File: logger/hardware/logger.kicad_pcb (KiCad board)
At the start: 4 copper layers, 56.6 x 27.9 mm, 44 parts, among them J2 USB_C_Receptacle_USB2.0_14P, J3 S5B-PH-SM4-TB(LF)(SN), J4 Conn_01x04, J5 Micro_SD_Card_Det2, Q1 2N7002K, SW1 SW_Push, SW2 SW_Push, U1 ESP32-S3-WROOM-1-N8, U2 TCAN330, U3 USBLC6-2P6, U4 TPS62172DSG

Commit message: Kicad updates and ignore
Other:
- board text added: "120 TERM"
- board text added: "BOOT"
- board text added: "RST"
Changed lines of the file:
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@@
 			(plot_on_all_layers_selection 0x00000000_00000000_00000000_00000000)
 			(disableapertmacros no)
-			(usegerberextensions no)
+			(usegerberextensions yes)
 			(usegerberattributes yes)
 			(usegerberadvancedattributes yes)
@@
 			(outputformat 1)
 			(mirror no)
-			(drillshape 1)
+			(drillshape 0)
 			(scaleselection 1)
 			(outputdirectory "")
@@
 			(at 3.646 -0.856 0)
 			(layer "F.SilkS")
+			(hide yes)
 			(effects
 				(font
@@
 			(at -0.89 2.344 0)
 			(layer "F.SilkS")
+			(hide yes)
 			(effects
 				(font
@@
 			)
 		)
-		(attr smd dnp)
+		(attr smd)
 		(duplicate_pad_numbers_are_jumpers no)
 		(fp_line
@@
 			(at 0 1.17 90)
 			(layer "B.SilkS")
+			(hide yes)
 			(effects
 				(font
@@
 		(layer "Edge.Cuts")
 	)
+	(gr_text "RST"
+		(at 146.7 82.6 0)
+		(layer "F.SilkS")
+		(effects
+			(font
+				(size 1 1)
+				(thickness 0.15)
+			)
+			(justify left bottom)
+		)
+	)
+	(gr_text "BOOT"
+		(at 131 81.9 90)
+		(layer "F.SilkS")
+		(effects
+			(font
+				(size 1 1)
+				(thickness 0.15)
+			)
+			(justify left bottom)
+		)
+	)
+	(gr_text "120\nTERM"
+		(at 121.315 81.5 0)
+		(layer "B.SilkS")
+		(effects
+			(font
+				(size 1 1)
+				(thickness 0.15)
+			)
+			(justify left bottom mirror)
+		)
+	)
 	(gr_text "3V3 OUT"

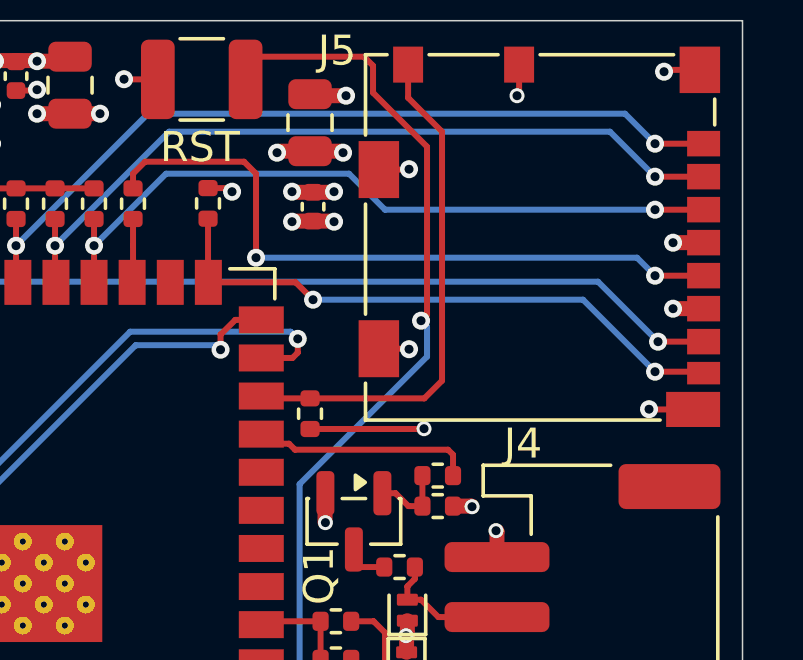
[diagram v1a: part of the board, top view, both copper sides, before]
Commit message: fix: I/O allocations on logger ESP32-S3
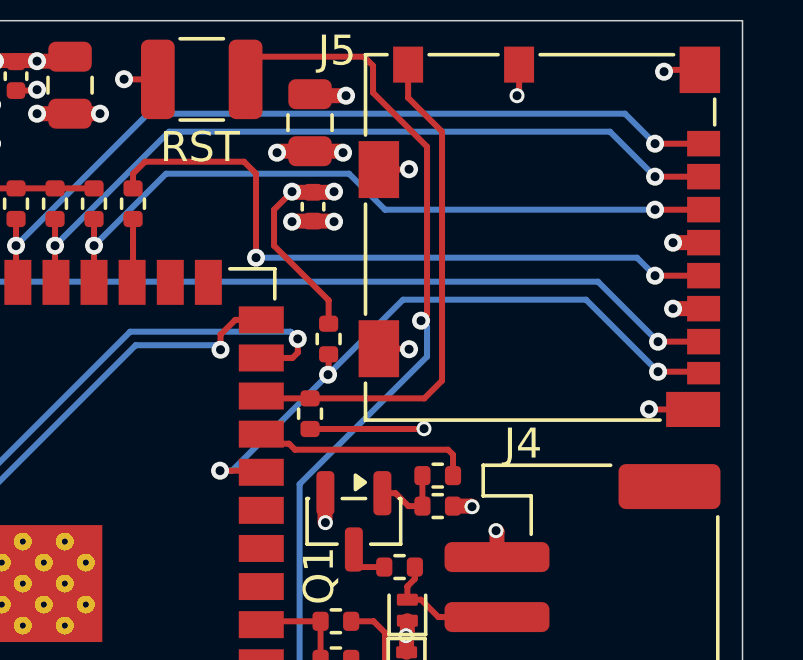
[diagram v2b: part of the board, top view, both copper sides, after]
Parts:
- U1: value ESP32-S3-WROOM-1-N8 -> ESP32-S3-WROOM-1-N4
- moved R11 6.05 mm to (152.3, 88.4)
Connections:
- U1 pad 10: unconnected-(U1-IO17-Pad10) -> Net-(J5-DAT1)
- U1 pad 15: Net-(J5-DAT1) -> unconnected-(U1-IO3-Pad15)
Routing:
- net +3.3V: track 31.0 -> 35.5 mm, vias 44 -> 43
- net Net-(J5-DAT1): track 19.9 -> 21.6 mm, vias 2 -> 3
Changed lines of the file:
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@@
 			(crossoutdnponfab yes)
 			(subtractmaskfromsilk no)
-			(outputformat 1)
+			(outputformat 4)
 			(mirror no)
 			(drillshape 0)
 			(scaleselection 1)
-			(outputdirectory "")
+			(outputdirectory "pdf")
 		)
 	)
@@
 	(footprint "Resistor_SMD:R_0402_1005Metric"
 		(layer "F.Cu")
-		(at 148.3 83.89 90)
+		(at 152.32 88.41 90)
 		(descr "Resistor SMD 0402 (1005 Metric), square (rectangular) end terminal, IPC-7351 nominal, (Body size source: IPC-SM-782 page 72, https://www.pcb-3d.com/wordpress/wp-content/uploads/ipc-sm-782a_amendment_1_and_2.pdf)")
 		(tags "resistor")
@@
 			)
 		)
-		(property "LCSC" "C7519"
+		(property "LCSC" "C15999"
 			(at 0 0 0)
 			(unlocked yes)
@@
 			)
 		)
-		(property "Value" "ESP32-S3-WROOM-1-N8"
+		(property "Value" "ESP32-S3-WROOM-1-N4"
 			(at 0 14.6 180)
 			(unlocked yes)
@@
 			)
 		)
-		(property "LCSC" "C2913198"
+		(property "LCSC" "C2913197"
 			(at 0 0 180)
 			(unlocked yes)
@@
 			(size 1.5 0.9)
 			(layers "F.Cu" "F.Mask" "F.Paste")
-			(net "unconnected-(U1-IO17-Pad10)")
+			(net "Net-(J5-DAT1)")
 			(pinfunction "IO17_10")
 			(pintype "bidirectional")
@@
 			(size 1.5 0.9)
 			(layers "F.Cu" "F.Mask" "F.Paste")
-			(net "Net-(J5-DAT1)")
+			(net "unconnected-(U1-IO3-Pad15)")
 			(pinfunction "IO3_15")
 			(pintype "bidirectional")
@@
 	)
 	(segment
-		(start 155.49 91.41)
-		(end 155.5 91.4)
+		(start 150.5 85.3)
+		(end 150.5 84.1)
 		(width 0.2)
 		(layer "F.Cu")
@@
 	)
 	(segment
-		(start 148.98 83.38)
-		(end 149.1 83.5)
+		(start 155.49 91.41)
+		(end 155.5 91.4)
 		(width 0.2)
 		(layer "F.Cu")
@@
 	)
 	(segment
+		(start 152.32 87.9)
+		(end 152.32 87.12)
+		(width 0.2)
+		(layer "F.Cu")
+		(net "+3.3V")
+	)
+	(segment
 		(start 151.7 91.41)
 		(end 155.49 91.41)
@@
 	)
 	(segment
-		(start 148.3 83.38)
-		(end 148.98 83.38)
+		(start 152.32 87.12)
+		(end 150.5 85.3)
+		(width 0.2)
+		(layer "F.Cu")
+		(net "+3.3V")
+	)
+	(segment
+		(start 150.5 84.1)
+		(end 151.1 83.5)
 		(width 0.2)
 		(layer "F.Cu")
@@
 	)
 	(via
-		(at 149.1 83.5)
-		(size 0.6)
-		(drill 0.3)
-		(layers "F.Cu" "B.Cu")
-		(net "+3.3V")
-	)
-	(via
 		(at 120.2 94.5)
 		(size 0.6)
@@
 	)
 	(segment
-		(start 148.3 86.5114)
-		(end 148.3106 86.522)
+		(start 152.32 89.58)
+		(end 152.3 89.6)
 		(width 0.2)
 		(layer "F.Cu")
@@
 	)
 	(segment
-		(start 164.771 89.5)
-		(end 164.819 89.548)
+		(start 163.3 89.5)
+		(end 164.771 89.5)
 		(width 0.2)
 		(layer "F.Cu")
@@
 	)
 	(segment
-		(start 151.8 87.1)
-		(end 151.222 86.522)
+		(start 150.0236 92.8)
+		(end 150.0756 92.852)
 		(width 0.2)
 		(layer "F.Cu")
@@
 	)
 	(segment
-		(start 151.222 86.522)
-		(end 148.3106 86.522)
+		(start 164.771 89.5)
+		(end 164.819 89.548)
 		(width 0.2)
 		(layer "F.Cu")
@@
 	)
 	(segment
-		(start 163.2 89.5)
-		(end 164.771 89.5)
+		(start 148.7 92.8)
+		(end 150.0236 92.8)
 		(width 0.2)
 		(layer "F.Cu")
@@
 	)
 	(segment
-		(start 148.3 84.4)
-		(end 148.3 86.5114)
+		(start 152.32 88.92)
+		(end 152.32 89.58)
 		(width 0.2)
 		(layer "F.Cu")
@@
 	)
 	(via
-		(at 163.2 89.5)
+		(at 163.3 89.5)
 		(size 0.6)
 		(drill 0.3)
@@
 	)
 	(via
-		(at 151.8 87.1)
+		(at 148.7 92.8)
 		(size 0.6)
 		(drill 0.3)
@@
 		(net "Net-(J5-DAT1)")
 	)
+	(via
+		(at 152.3 89.6)
+		(size 0.6)
+		(drill 0.3)
+		(layers "F.Cu" "B.Cu")
+		(net "Net-(J5-DAT1)")
+	)
+	(segment
+		(start 149.1 92.8)
+		(end 148.7 92.8)
+		(width 0.2)
+		(layer "B.Cu")
+		(net "Net-(J5-DAT1)")
+	)
+	(segment
+		(start 152.3 89.6)
+		(end 154.8 87.1)
+		(width 0.2)
+		(layer "B.Cu")
+		(net "Net-(J5-DAT1)")
+	)
+	(segment
+		(start 154.8 87.1)
+		(end 160.9 87.1)
+		(width 0.2)
+		(layer "B.Cu")
+		(net "Net-(J5-DAT1)")
+	)
 	(segment
-		(start 160.8 87.1)
-		(end 163.2 89.5)
+		(start 152.3 89.6)
+		(end 149.1 92.8)
 		(width 0.2)
 		(layer "B.Cu")
@@
 	)
 	(segment
-		(start 151.8 87.1)
-		(end 160.8 87.1)
+		(start 160.9 87.1)
+		(end 163.3 89.5)
 		(width 0.2)
 		(layer "B.Cu")

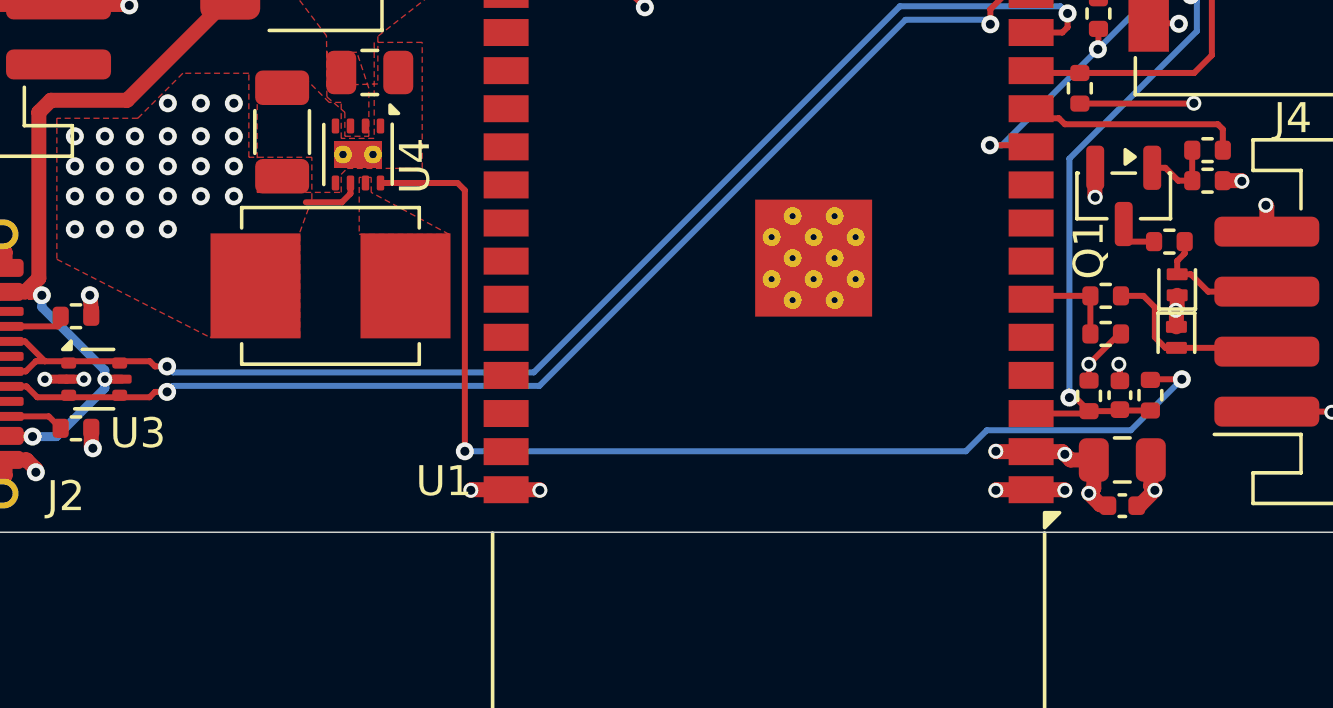
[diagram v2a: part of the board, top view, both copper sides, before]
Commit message: Logger: Add LEDs, connector silk, layout updates
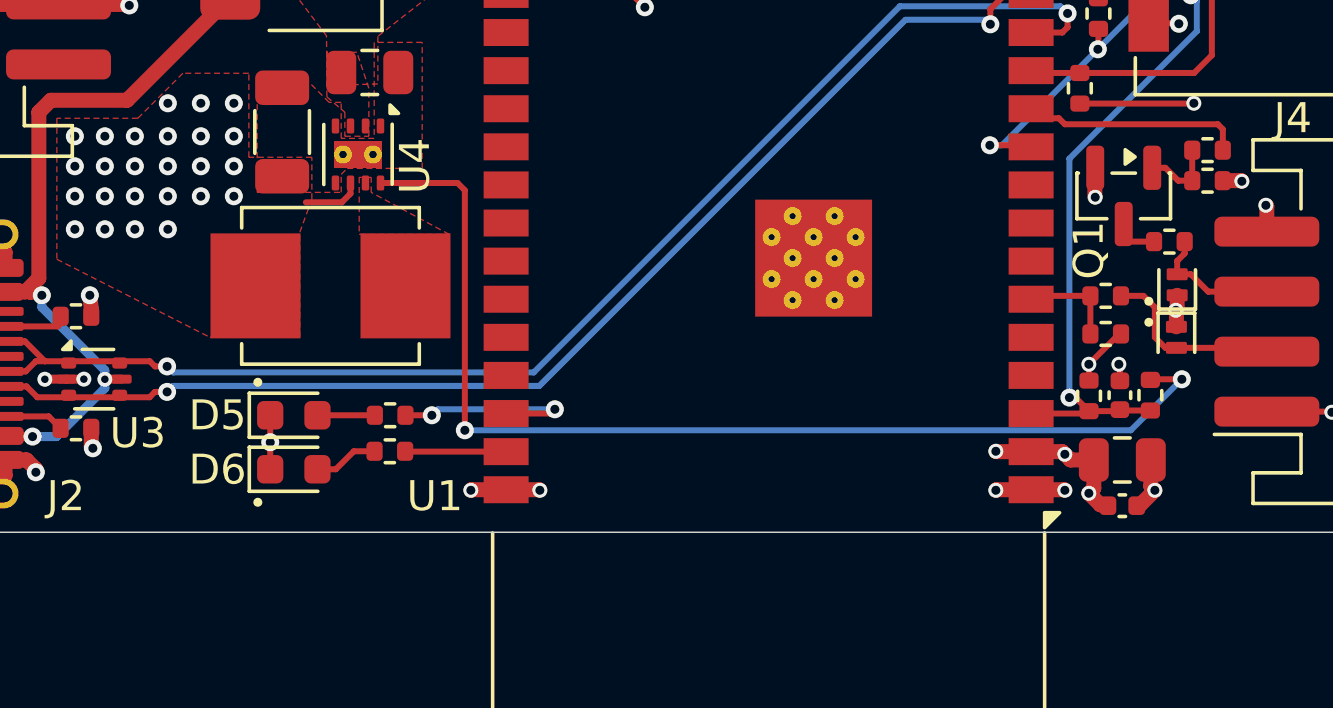
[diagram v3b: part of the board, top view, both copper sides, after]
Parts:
- added D5: GRN, LED_SMD:LED_0603_1608Metric, F.Cu at (125.5, 101.8)
- added D6: RED, LED_SMD:LED_0603_1608Metric, F.Cu at (125.5, 103.6)
- added R20: 100, Resistor_SMD:R_0402_1005Metric, F.Cu at (128.7, 101.8)
- added R21: 100, Resistor_SMD:R_0402_1005Metric, F.Cu at (128.7, 103.0)
- R4: value 47 -> 100
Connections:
- U1 pad 38: unconnected-(U1-IO2-Pad38) -> Net-(U1-IO2)
- U1 pad 39: unconnected-(U1-IO1-Pad39) -> Net-(U1-IO1)
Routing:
- net Net-(U1-IO2): track 0.00 -> 6.75 mm, vias 0 -> 2
- net Net-(U1-IO1): track 0.00 -> 3.37 mm
- net Net-(D6-A): track 0.00 -> 2.15 mm
- net Net-(D5-A): track 0.00 -> 1.91 mm
- net GND: track 45.7 -> 47.5 mm, vias 36 -> 37
- net Net-(U4-PG): track 37.6 -> 36.6 mm
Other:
- board text added: "12V-IN"
- board text added: "3.3V"
- board text added: "CAN-H"
- board text added: "CAN-L"
- board text added: "GND"
- board text added: "LOG/TRANSMITTER"
- board text added: "NC"
- board text added: "OPEN-CHMBL"
- board text added: "REV A"

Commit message: Logger: Add UART test pads
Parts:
- added TP1: RX, TestPoint:TestPoint_Pad_2.0x2.0mm, B.Cu at (136.0, 90.5)
- added TP2: TX, TestPoint:TestPoint_Pad_2.0x2.0mm, B.Cu at (132.0, 90.5)
- added TP3: GND, TestPoint:TestPoint_Pad_2.0x2.0mm, B.Cu at (128.0, 90.5)
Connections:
- U1 pad 36: unconnected-(U1-RXD0-Pad36) -> Net-(U1-RXD0)
- U1 pad 37: unconnected-(U1-TXD0-Pad37) -> Net-(U1-TXD0)
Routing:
- net Net-(U1-TXD0): track 0.00 -> 14.2 mm, vias 0 -> 1
- net Net-(U1-RXD0): track 0.00 -> 11.3 mm, vias 0 -> 1
- net GND: track 47.5 -> 50.3 mm, vias 37 -> 38
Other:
- board text added: "RXD"
- board text added: "TXD"

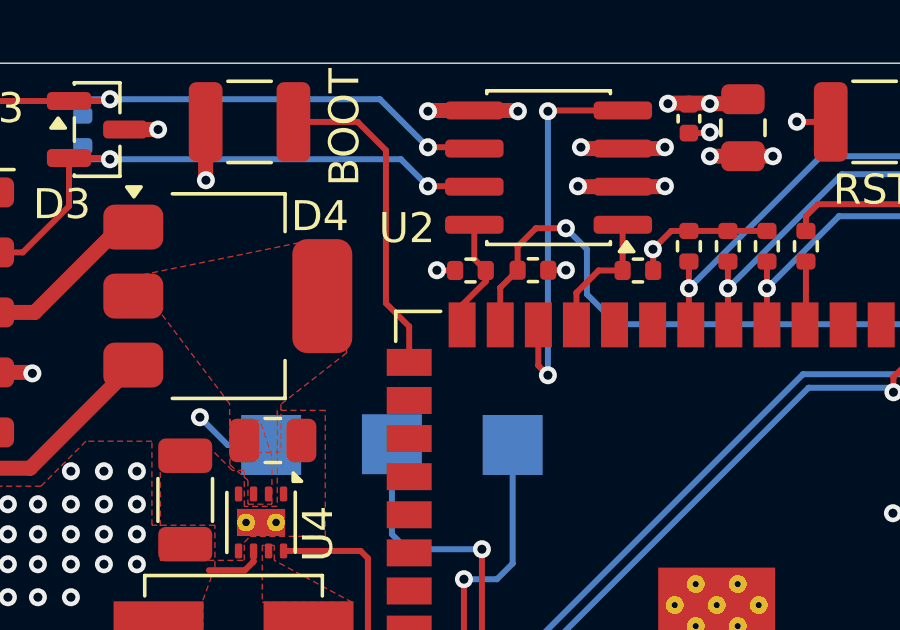
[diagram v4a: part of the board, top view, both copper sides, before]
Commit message: Logger: Fix GPIO45 usage
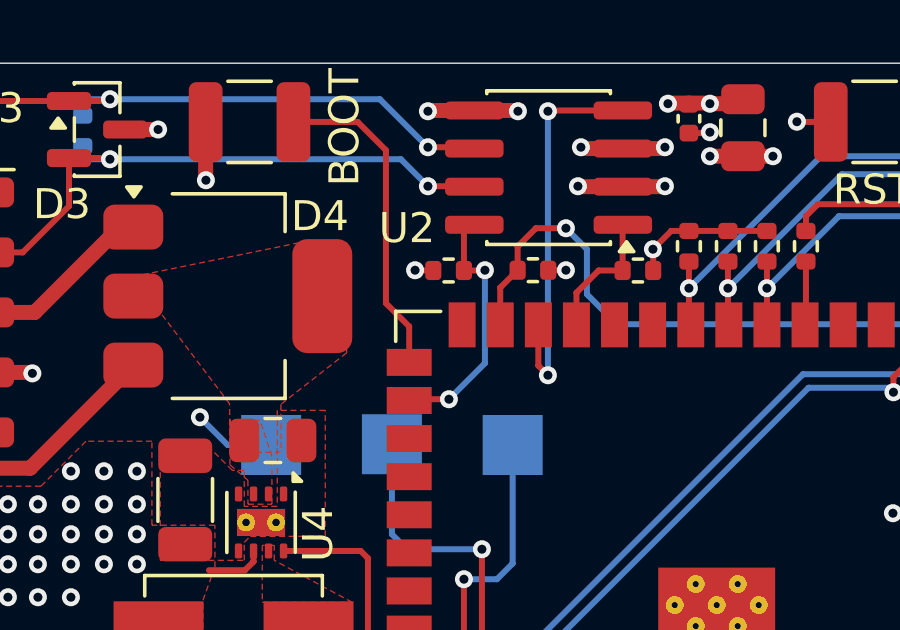
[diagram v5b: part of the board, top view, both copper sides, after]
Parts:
- moved R16 0.73 mm to (133.9, 84.7)
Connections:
- R16 pad 2: Net-(U1-IO45) -> Net-(U1-IO35)
- U1 pad 26: Net-(U1-IO45) -> unconnected-(U1-IO45-Pad26)
- U1 pad 28: unconnected-(U1-IO35-Pad28) -> Net-(U1-IO35)
- U2 pad 8: Net-(U1-IO45) -> Net-(U1-IO35)
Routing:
- net Net-(U1-IO35): track 0.00 -> 8.70 mm, vias 0 -> 2
- net Net-(U1-IO45): track 3.82 -> 0.00 mm
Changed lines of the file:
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@@
 	(footprint "Resistor_SMD:R_0402_1005Metric"
 		(layer "F.Cu")
-		(at 134.618 84.709)
+		(at 133.89 84.709)
 		(descr "Resistor SMD 0402 (1005 Metric), square (rectangular) end terminal, IPC-7351 nominal, (Body size source: IPC-SM-782 page 72, https://www.pcb-3d.com/wordpress/wp-content/uploads/ipc-sm-782a_amendment_1_and_2.pdf)")
 		(tags "resistor")
@@
 			(layers "F.Cu" "F.Mask" "F.Paste")
 			(roundrect_rratio 0.25)
-			(net "Net-(U1-IO45)")
+			(net "Net-(U1-IO35)")
 			(pintype "passive")
 		)
@@
 			(size 1.5 0.9)
 			(layers "F.Cu" "F.Mask" "F.Paste")
-			(net "Net-(U1-IO45)")
+			(net "unconnected-(U1-IO45-Pad26)")
 			(pinfunction "IO45_26")
 			(pintype "bidirectional")
@@
 			(size 1.5 0.9)
 			(layers "F.Cu" "F.Mask" "F.Paste")
-			(net "unconnected-(U1-IO35-Pad28)")
+			(net "Net-(U1-IO35)")
 			(pinfunction "IO35_28")
 			(pintype "bidirectional")
@@
 			(layers "F.Cu" "F.Mask" "F.Paste")
 			(roundrect_rratio 0.25)
-			(net "Net-(U1-IO45)")
+			(net "Net-(U1-IO35)")
 			(pinfunction "S_8")
 			(pintype "input")
@@
 	)
 	(segment
-		(start 133.509 84.709)
-		(end 133.5 84.7)
+		(start 132.781 84.709)
+		(end 132.772 84.7)
 		(width 0.2)
 		(layer "F.Cu")
@@
 	)
 	(segment
-		(start 134.108 84.709)
-		(end 133.509 84.709)
+		(start 133.38 84.709)
+		(end 132.781 84.709)
 		(width 0.2)
 		(layer "F.Cu")
@@
 	)
 	(via
-		(at 133.5 84.7)
+		(at 132.772 84.7)
 		(size 0.6)
 		(drill 0.3)
@@
 	)
 	(segment
-		(start 134.3406 85.8594)
-		(end 134.3406 86.522)
-		(width 0.2)
-		(layer "F.Cu")
-		(net "Net-(U1-IO45)")
-	)
-	(segment
-		(start 134.747 83.185)
-		(end 134.747 84.328)
-		(width 0.2)
-		(layer "F.Cu")
-		(net "Net-(U1-IO45)")
-	)
-	(segment
-		(start 135.128 84.709)
-		(end 135.128 85.072)
-		(width 0.2)
-		(layer "F.Cu")
-		(net "Net-(U1-IO45)")
-	)
-	(segment
-		(start 134.747 84.328)
-		(end 135.128 84.709)
-		(width 0.2)
-		(layer "F.Cu")
-		(net "Net-(U1-IO45)")
-	)
-	(segment
-		(start 135.128 85.072)
-		(end 134.3406 85.8594)
-		(width 0.2)
-		(layer "F.Cu")
-		(net "Net-(U1-IO45)")
-	)
-	(segment
 		(start 126.2875 101.8)
 		(end 128.2 101.8)
@@
 		(net "Net-(U1-TXD0)")
 	)
+	(segment
+		(start 135.091 84.709)
+		(end 135.1 84.7)
+		(width 0.2)
+		(layer "F.Cu")
+		(net "Net-(U1-IO35)")
+	)
+	(segment
+		(start 134.747 83.185)
+		(end 134.415 83.185)
+		(width 0.2)
+		(layer "F.Cu")
+		(net "Net-(U1-IO35)")
+	)
+	(segment
+		(start 133.9 89)
+		(end 132.6176 89)
+		(width 0.2)
+		(layer "F.Cu")
+		(net "Net-(U1-IO35)")
+	)
+	(segment
+		(start 134.4 84.709)
+		(end 135.091 84.709)
+		(width 0.2)
+		(layer "F.Cu")
+		(net "Net-(U1-IO35)")
+	)
+	(segment
+		(start 132.6176 89)
+		(end 132.5756 89.042)
+		(width 0.2)
+		(layer "F.Cu")
+		(net "Net-(U1-IO35)")
+	)
+	(segment
+		(start 134.4 83.2)
+		(end 134.4 84.709)
+		(width 0.2)
+		(layer "F.Cu")
+		(net "Net-(U1-IO35)")
+	)
+	(segment
+		(start 134.415 83.185)
+		(end 134.4 83.2)
+		(width 0.2)
+		(layer "F.Cu")
+		(net "Net-(U1-IO35)")
+	)
+	(via
+		(at 133.9 89)
+		(size 0.6)
+		(drill 0.3)
+		(layers "F.Cu" "B.Cu")
+		(net "Net-(U1-IO35)")
+	)
+	(via
+		(at 135.1 84.7)
+		(size 0.6)
+		(drill 0.3)
+		(layers "F.Cu" "B.Cu")
+		(net "Net-(U1-IO35)")
+	)
+	(segment
+		(start 135.1 84.7)
+		(end 135.1 87.8)
+		(width 0.2)
+		(layer "B.Cu")
+		(net "Net-(U1-IO35)")
+	)
+	(segment
+		(start 135.1 87.8)
+		(end 133.9 89)
+		(width 0.2)
+		(layer "B.Cu")
+		(net "Net-(U1-IO35)")
+	)
 	(zone

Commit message: Logger: Switch to TPS62162DSGR with 1A output rating
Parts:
- U4: value TPS62172DSG -> TPS62162DSGR
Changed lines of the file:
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@@
 			)
 		)
-		(property "Value" "TPS62172DSG"
+		(property "Value" "TPS62162DSGR"
 			(at 0.01 2.14 90)
 			(layer "F.Fab")
@@
 			)
 		)
-		(property "LCSC" "C59873"
+		(property "LCSC" "C40256"
 			(at 0 0 270)
 			(unlocked yes)
